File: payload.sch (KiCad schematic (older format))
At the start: 26 parts, among them J11 JST-PA-2, J12 JST-PA-2, J14 JST-PA-2, J15 JST-PA-2, J23 JST-PA-2, J24 JST-PA-2, Q5 IRFZ44, Q6 IRFZ44, U14 74LS74, U15 74LS74

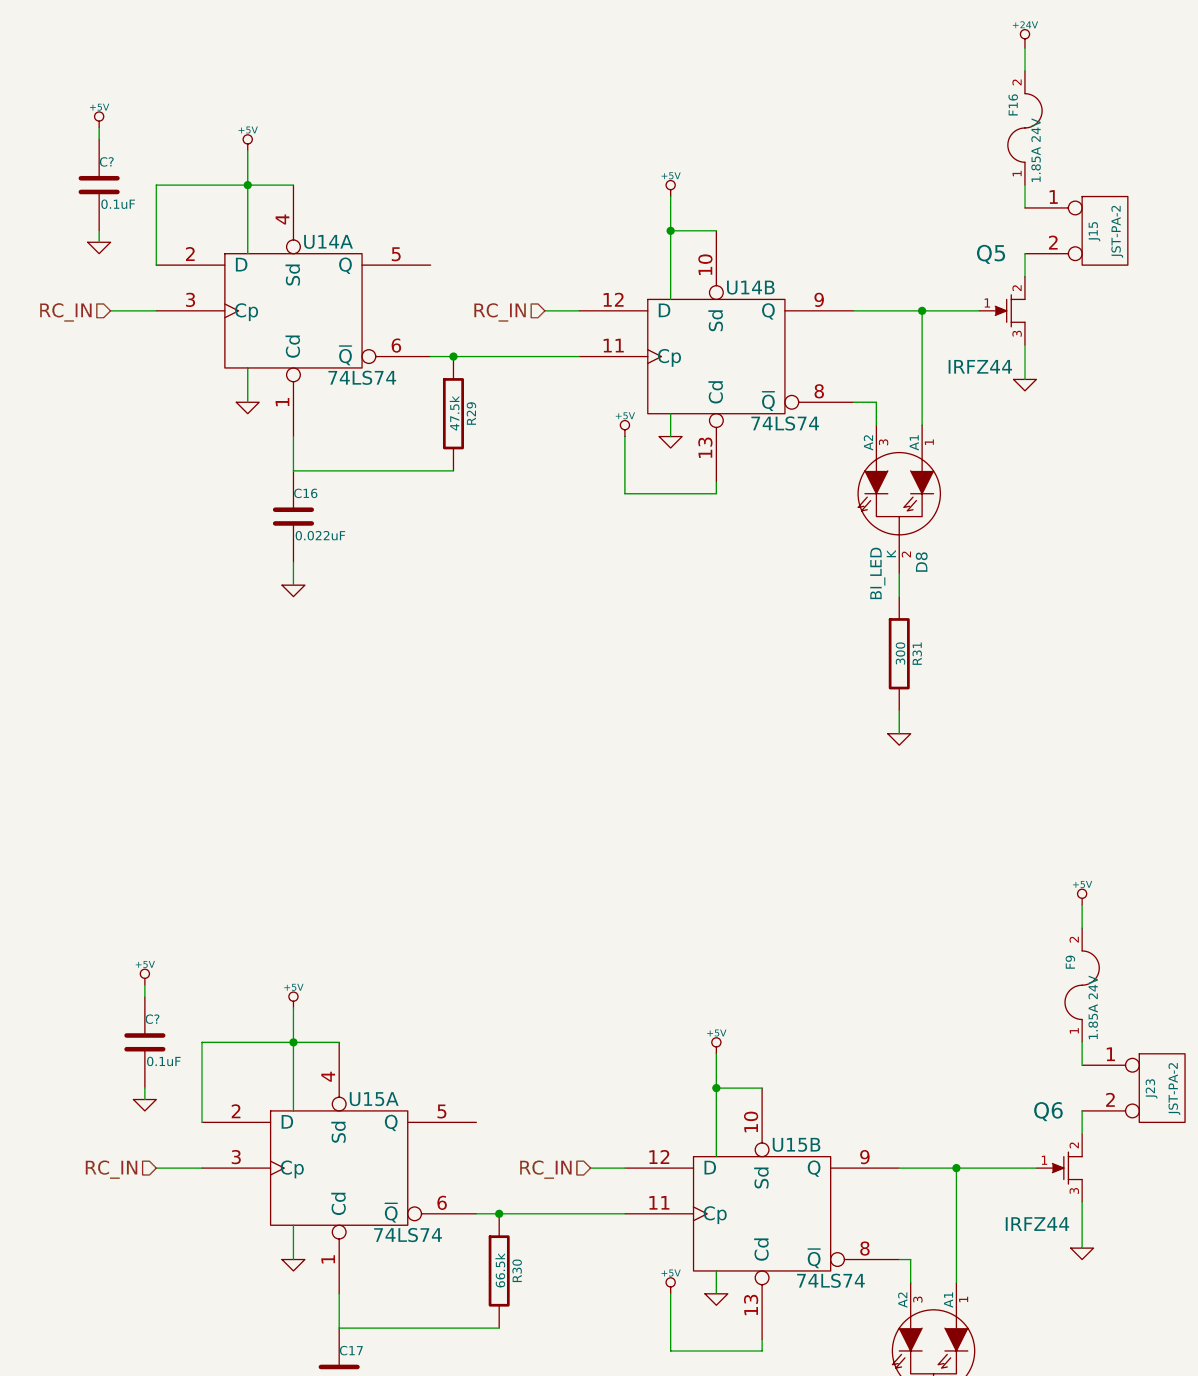
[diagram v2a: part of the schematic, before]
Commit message: Adding buffer on voltage reference output.
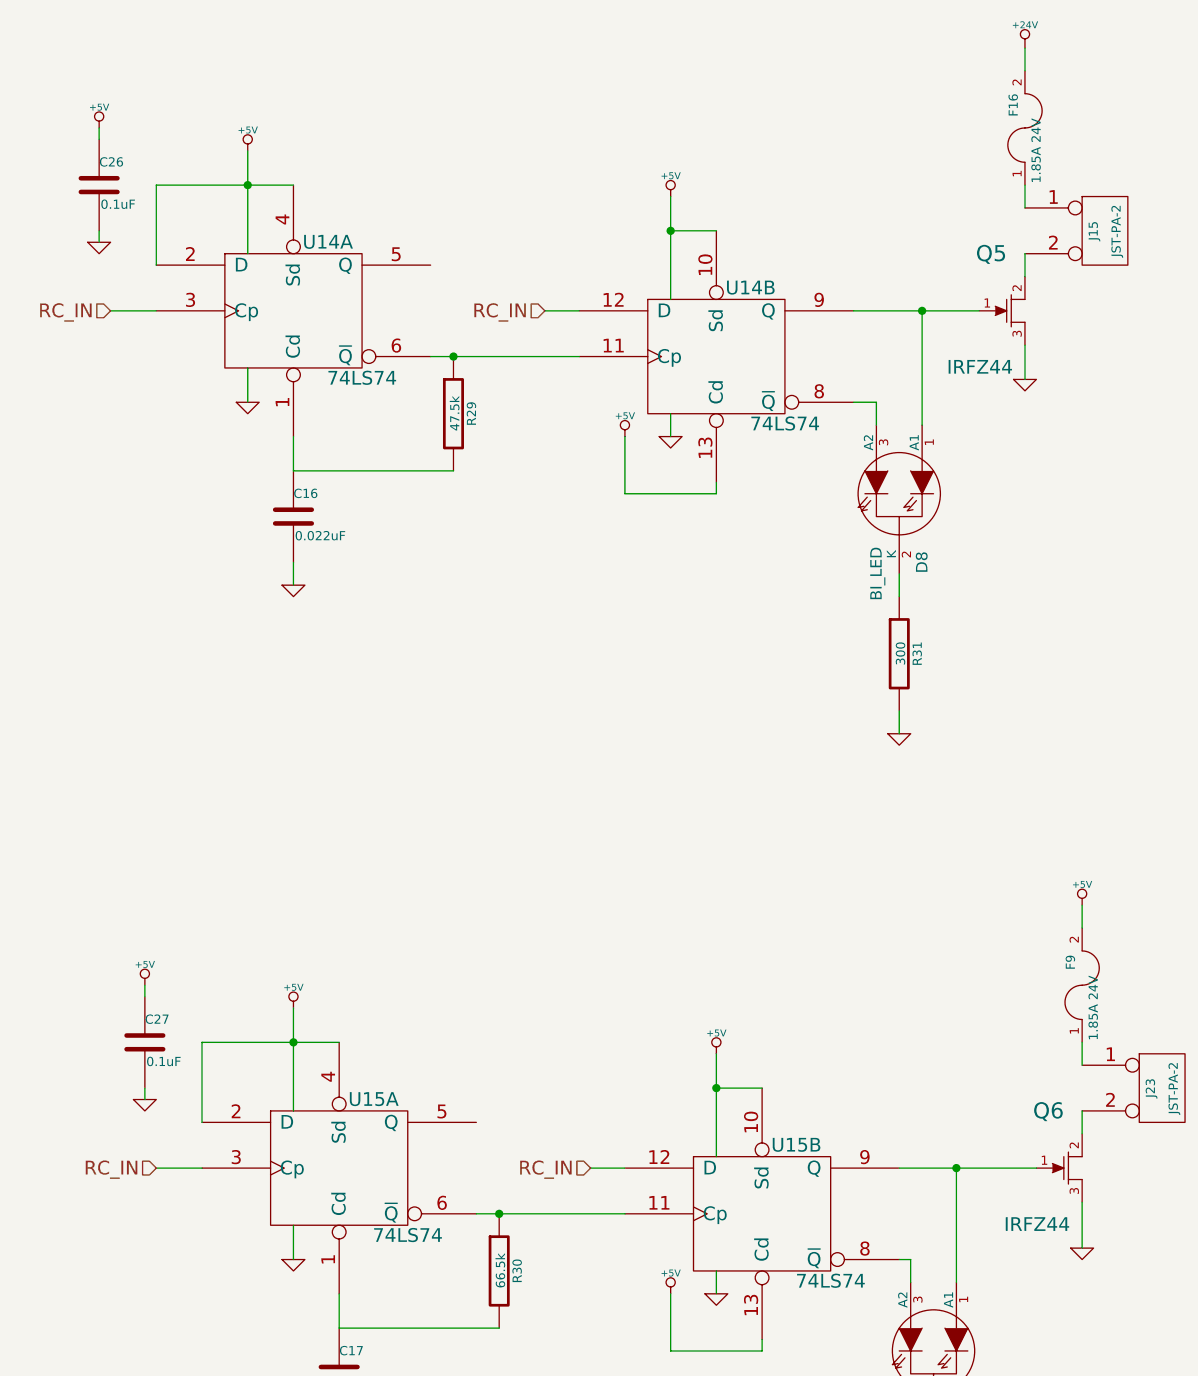
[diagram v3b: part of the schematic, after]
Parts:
- gave numbers to parts that had none: 2
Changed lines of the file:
@@
 $EndComp
 $Comp
-L +5V #PWR089
+L +5V #PWR0111
 U 1 1 55CD3D65
 P 3750 5100
-F 0 "#PWR089" H 3750 5190 20  0001 C CNN
+F 0 "#PWR0111" H 3750 5190 20  0001 C CNN
 F 1 "+5V" H 3750 5190 30  0000 C CNN
 F 2 "" H 3750 5100 60  0000 C CNN
@@
 $EndComp
 $Comp
-L +5V #PWR090
+L +5V #PWR0112
 U 1 1 55CD3D6B
 P 1900 4900
-F 0 "#PWR090" H 1900 4990 20  0001 C CNN
+F 0 "#PWR0112" H 1900 4990 20  0001 C CNN
 F 1 "+5V" H 1900 4990 30  0000 C CNN
 F 2 "" H 1900 4900 60  0000 C CNN
@@
 $EndComp
 $Comp
-L GND #PWR091
+L GND #PWR0113
 U 1 1 55D6B0A7
 P 2100 6800
-F 0 "#PWR091" H 2100 6800 30  0001 C CNN
+F 0 "#PWR0113" H 2100 6800 30  0001 C CNN
 F 1 "GND" H 2100 6730 30  0001 C CNN
 F 2 "" H 2100 6800 60  0000 C CNN
@@
 $EndComp
 $Comp
-L +5V #PWR092
+L +5V #PWR0114
 U 1 1 55D6B0A9
 P 3550 6150
-F 0 "#PWR092" H 3550 6240 20  0001 C CNN
+F 0 "#PWR0114" H 3550 6240 20  0001 C CNN
 F 1 "+5V" H 3550 6240 30  0000 C CNN
 F 2 "" H 3550 6150 60  0000 C CNN
@@
 $EndComp
 $Comp
-L GND #PWR093
+L GND #PWR0115
 U 1 1 55D6B0AD
 P 1900 6000
-F 0 "#PWR093" H 1900 6000 30  0001 C CNN
+F 0 "#PWR0115" H 1900 6000 30  0001 C CNN
 F 1 "GND" H 1900 5930 30  0001 C CNN
 F 2 "" H 1900 6000 60  0000 C CNN
@@
 $EndComp
 $Comp
-L GND #PWR094
+L GND #PWR0116
 U 1 1 55D6B0AF
 P 3750 6150
-F 0 "#PWR094" H 3750 6150 30  0001 C CNN
+F 0 "#PWR0116" H 3750 6150 30  0001 C CNN
 F 1 "GND" H 3750 6080 30  0001 C CNN
 F 2 "" H 3750 6150 60  0000 C CNN
@@
 $EndComp
 $Comp
-L +5V #PWR095
+L +5V #PWR0117
 U 1 1 55D6B0B9
 P 3550 1350
-F 0 "#PWR095" H 3550 1440 20  0001 C CNN
+F 0 "#PWR0117" H 3550 1440 20  0001 C CNN
 F 1 "+5V" H 3550 1440 30  0000 C CNN
 F 2 "" H 3550 1350 60  0000 C CNN
@@
 $EndComp
 $Comp
-L +5V #PWR096
+L +5V #PWR0118
 U 1 1 55CD3F45
 P 1700 1150
-F 0 "#PWR096" H 1700 1240 20  0001 C CNN
+F 0 "#PWR0118" H 1700 1240 20  0001 C CNN
 F 1 "+5V" H 1700 1240 30  0000 C CNN
 F 2 "" H 1700 1150 60  0000 C CNN
@@
 $EndComp
 $Comp
-L GND #PWR097
+L GND #PWR0119
 U 1 1 55D6B0C1
 P 1900 3050
-F 0 "#PWR097" H 1900 3050 30  0001 C CNN
+F 0 "#PWR0119" H 1900 3050 30  0001 C CNN
 F 1 "GND" H 1900 2980 30  0001 C CNN
 F 2 "" H 1900 3050 60  0000 C CNN
@@
 $EndComp
 $Comp
-L +5V #PWR098
+L +5V #PWR0120
 U 1 1 55D6B0C2
 P 3350 2400
-F 0 "#PWR098" H 3350 2490 20  0001 C CNN
+F 0 "#PWR0120" H 3350 2490 20  0001 C CNN
 F 1 "+5V" H 3350 2490 30  0000 C CNN
 F 2 "" H 3350 2400 60  0000 C CNN
@@
 $EndComp
 $Comp
-L GND #PWR099
+L GND #PWR0121
 U 1 1 55CD3F87
 P 1700 2250
-F 0 "#PWR099" H 1700 2250 30  0001 C CNN
+F 0 "#PWR0121" H 1700 2250 30  0001 C CNN
 F 1 "GND" H 1700 2180 30  0001 C CNN
 F 2 "" H 1700 2250 60  0000 C CNN
@@
 $EndComp
 $Comp
-L GND #PWR0100
+L GND #PWR0122
 U 1 1 55CD3F8E
 P 3550 2400
-F 0 "#PWR0100" H 3550 2400 30  0001 C CNN
+F 0 "#PWR0122" H 3550 2400 30  0001 C CNN
 F 1 "GND" H 3550 2330 30  0001 C CNN
 F 2 "" H 3550 2400 60  0000 C CNN
@@
 $EndComp
 $Comp
-L GND #PWR0101
+L GND #PWR0123
 U 1 1 55CD4B0A
 P 4550 3700
-F 0 "#PWR0101" H 4550 3700 30  0001 C CNN
+F 0 "#PWR0123" H 4550 3700 30  0001 C CNN
 F 1 "GND" H 4550 3630 30  0001 C CNN
 F 2 "" H 4550 3700 60  0000 C CNN
@@
 $EndComp
 $Comp
-L GND #PWR0102
+L GND #PWR0124
 U 1 1 55D6B0D9
 P 4700 7450
-F 0 "#PWR0102" H 4700 7450 30  0001 C CNN
+F 0 "#PWR0124" H 4700 7450 30  0001 C CNN
 F 1 "GND" H 4700 7380 30  0001 C CNN
 F 2 "" H 4700 7450 60  0000 C CNN
@@
 $EndComp
 $Comp
-L GND #PWR0103
+L GND #PWR0125
 U 1 1 55D66B70
 P 5350 5950
-F 0 "#PWR0103" H 5350 5950 30  0001 C CNN
+F 0 "#PWR0125" H 5350 5950 30  0001 C CNN
 F 1 "GND" H 5350 5880 30  0001 C CNN
 F 2 "" H 5350 5950 60  0000 C CNN
@@
 $EndComp
 $Comp
-L +5V #PWR0104
+L +5V #PWR0126
 U 1 1 55D66CB9
 P 5350 4450
-F 0 "#PWR0104" H 5350 4540 20  0001 C CNN
+F 0 "#PWR0126" H 5350 4540 20  0001 C CNN
 F 1 "+5V" H 5350 4540 30  0000 C CNN
 F 2 "" H 5350 4450 60  0000 C CNN
@@
 $EndComp
 $Comp
-L GND #PWR0105
+L GND #PWR0127
 U 1 1 55D66D5E
 P 5100 2150
-F 0 "#PWR0105" H 5100 2150 30  0001 C CNN
+F 0 "#PWR0127" H 5100 2150 30  0001 C CNN
 F 1 "GND" H 5100 2080 30  0001 C CNN
 F 2 "" H 5100 2150 60  0000 C CNN
@@
 $EndComp
 $Comp
-L +24V #PWR0106
+L +24V #PWR0128
 U 1 1 55D66E1E
 P 5100 700
-F 0 "#PWR0106" H 5100 650 20  0001 C CNN
+F 0 "#PWR0128" H 5100 650 20  0001 C CNN
 F 1 "+24V" H 5100 800 30  0000 C CNN
 F 2 "" H 5100 700 60  0000 C CNN
@@
 	3750 2600 3750 2650
 Wire Wire Line
-	4350 1850 4650 1850
-Wire Wire Line
-	4650 1850 4900 1850
+	4350 1850 4900 1850
 Wire Wire Line
 	3150 1850 3000 1850
@@
 Connection ~ 2600 2050
 Wire Wire Line
-	2500 2050 2600 2050
-Wire Wire Line
-	2600 2050 3150 2050
+	2500 2050 3150 2050
 Wire Wire Line
 	1900 2550 1900 2400
@@
 Connection ~ 1700 1300
 Wire Wire Line
-	1300 1300 1700 1300
-Wire Wire Line
-	1700 1300 1900 1300
-Wire Wire Line
-	3550 1350 3550 1500
-Wire Wire Line
-	3550 1500 3550 1800
-Wire Wire Line
-	1700 1150 1700 1300
-Wire Wire Line
-	1700 1300 1700 1600
+	1300 1300 1900 1300
+Wire Wire Line
+	3550 1350 3550 1800
+Wire Wire Line
+	1700 1150 1700 1600
 Wire Wire Line
 	3750 6050 3750 6150
@@
 	3950 6350 3950 6400
 Wire Wire Line
-	4550 5600 4800 5600
-Wire Wire Line
-	4800 5600 5150 5600
+	4550 5600 5150 5600
 Wire Wire Line
 	3350 5600 3200 5600
@@
 Connection ~ 2800 5800
 Wire Wire Line
-	2700 5800 2800 5800
-Wire Wire Line
-	2800 5800 3350 5800
+	2700 5800 3350 5800
 Wire Wire Line
 	2100 6300 2100 6150
@@
 Connection ~ 1900 5050
 Wire Wire Line
-	1500 5050 1900 5050
-Wire Wire Line
-	1900 5050 2100 5050
-Wire Wire Line
-	3750 5100 3750 5250
-Wire Wire Line
-	3750 5250 3750 5550
-Wire Wire Line
-	1900 4900 1900 5050
-Wire Wire Line
-	1900 5050 1900 5350
-$Comp
-L GND #PWR0107
+	1500 5050 2100 5050
+Wire Wire Line
+	3750 5100 3750 5550
+Wire Wire Line
+	1900 4900 1900 5350
+$Comp
+L GND #PWR0129
 U 1 1 55D66E73
 P 7950 6850
-F 0 "#PWR0107" H 7950 6850 30  0001 C CNN
+F 0 "#PWR0129" H 7950 6850 30  0001 C CNN
 F 1 "GND" H 7950 6780 30  0001 C CNN
 F 2 "" H 7950 6850 60  0000 C CNN
@@
 $EndComp
 $Comp
-L +5V #PWR0108
+L +5V #PWR0130
 U 1 1 55D66E7F
 P 7300 6500
-F 0 "#PWR0108" H 7300 6590 20  0001 C CNN
+F 0 "#PWR0130" H 7300 6590 20  0001 C CNN
 F 1 "+5V" H 7300 6590 30  0000 C CNN
 F 2 "" H 7300 6500 60  0000 C CNN
@@
 	7300 6550 7300 6500
 $Comp
-L GND #PWR0109
+L GND #PWR0131
 U 1 1 55D66F4E
 P 9300 6850
-F 0 "#PWR0109" H 9300 6850 30  0001 C CNN
+F 0 "#PWR0131" H 9300 6850 30  0001 C CNN
 F 1 "GND" H 9300 6780 30  0001 C CNN
 F 2 "" H 9300 6850 60  0000 C CNN
@@
 $EndComp
 $Comp
-L +5V #PWR0110
+L +5V #PWR0132
 U 1 1 55D66F5A
 P 8650 6500
-F 0 "#PWR0110" H 8650 6590 20  0001 C CNN
+F 0 "#PWR0132" H 8650 6590 20  0001 C CNN
 F 1 "+5V" H 8650 6590 30  0000 C CNN
 F 2 "" H 8650 6500 60  0000 C CNN
@@
 	8650 6550 8650 6500
 $Comp
-L GND #PWR0111
+L GND #PWR0133
 U 1 1 55D66F6A
 P 9300 6100
-F 0 "#PWR0111" H 9300 6100 30  0001 C CNN
+F 0 "#PWR0133" H 9300 6100 30  0001 C CNN
 F 1 "GND" H 9300 6030 30  0001 C CNN
 F 2 "" H 9300 6100 60  0000 C CNN
@@
 $EndComp
 $Comp
-L GND #PWR0112
+L GND #PWR0134
 U 1 1 55D66F86
 P 7950 6100
-F 0 "#PWR0112" H 7950 6100 30  0001 C CNN
+F 0 "#PWR0134" H 7950 6100 30  0001 C CNN
 F 1 "GND" H 7950 6030 30  0001 C CNN
 F 2 "" H 7950 6100 60  0000 C CNN
@@
 	7300 5800 7300 5750
 $Comp
-L +24V #PWR0113
+L +24V #PWR0135
 U 1 1 55D66F9C
 P 7300 5750
-F 0 "#PWR0113" H 7300 5700 20  0001 C CNN
+F 0 "#PWR0135" H 7300 5700 20  0001 C CNN
 F 1 "+24V" H 7300 5850 30  0000 C CNN
 F 2 "" H 7300 5750 60  0000 C CNN
@@
 $EndComp
 $Comp
-L +24V #PWR0114
+L +24V #PWR0136
 U 1 1 55D66FA2
 P 8650 5750
-F 0 "#PWR0114" H 8650 5700 20  0001 C CNN
+F 0 "#PWR0136" H 8650 5700 20  0001 C CNN
 F 1 "+24V" H 8650 5850 30  0000 C CNN
 F 2 "" H 8650 5750 60  0000 C CNN
@@
 $EndComp
 $Comp
-L C C?
+L C C26
 U 1 1 55D80A93
 P 1050 1300
-F 0 "C?" H 1050 1400 40  0000 L CNN
+F 0 "C26" H 1050 1400 40  0000 L CNN
 F 1 "0.1uF" H 1056 1215 40  0000 L CNN
 F 2 "SM0805" H 1088 1150 30  0001 C CNN
@@
 $EndComp
 $Comp
-L +5V #PWR?
+L +5V #PWR0137
 U 1 1 55D80A99
 P 1050 1050
-F 0 "#PWR?" H 1050 1140 20  0001 C CNN
+F 0 "#PWR0137" H 1050 1140 20  0001 C CNN
 F 1 "+5V" H 1050 1140 30  0000 C CNN
 F 2 "" H 1050 1050 60  0000 C CNN
@@
 $EndComp
 $Comp
-L GND #PWR?
+L GND #PWR0138
 U 1 1 55D80A9F
 P 1050 1550
-F 0 "#PWR?" H 1050 1550 30  0001 C CNN
+F 0 "#PWR0138" H 1050 1550 30  0001 C CNN
 F 1 "GND" H 1050 1480 30  0001 C CNN
 F 2 "" H 1050 1550 60  0000 C CNN
@@
 	1050 1100 1050 1050
 $Comp
-L C C?
+L C C27
 U 1 1 55D80ABD
 P 1250 5050
-F 0 "C?" H 1250 5150 40  0000 L CNN
+F 0 "C27" H 1250 5150 40  0000 L CNN
 F 1 "0.1uF" H 1256 4965 40  0000 L CNN
 F 2 "SM0805" H 1288 4900 30  0001 C CNN
@@
 $EndComp
 $Comp
-L +5V #PWR?
+L +5V #PWR0139
 U 1 1 55D80AC3
 P 1250 4800
-F 0 "#PWR?" H 1250 4890 20  0001 C CNN
+F 0 "#PWR0139" H 1250 4890 20  0001 C CNN
 F 1 "+5V" H 1250 4890 30  0000 C CNN
 F 2 "" H 1250 4800 60  0000 C CNN
@@
 $EndComp
 $Comp
-L GND #PWR?
+L GND #PWR0140
 U 1 1 55D80AC9
 P 1250 5300
-F 0 "#PWR?" H 1250 5300 30  0001 C CNN
+F 0 "#PWR0140" H 1250 5300 30  0001 C CNN
 F 1 "GND" H 1250 5230 30  0001 C CNN
 F 2 "" H 1250 5300 60  0000 C CNN
